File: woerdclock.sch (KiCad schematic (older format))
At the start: 50 parts, among them K1 Sound, K2 IR, K3 CONN_3, K4 CONN_3, P1 Jumper, P2 Jumper, P3 Jumper, P4 CONN_1, P5 CONN_1, P6 CONN_1, P7 CONN_1, SW1 up, SW2 ok, SW3 down, U1 RFM12B, U10 DCF77, U11 DHT, U14 SD-CARD, U2 RTC_MODUL, U3 ARDUINO_MINI_PRO, U6 HC-05, U7 HC-05, U8 ESP8266, U9 10DOF

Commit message: sub-PCBs ready.
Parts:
- removed K4: CONN_3, symbol CONN_3
- removed U3: ARDUINO_MINI_PRO, symbol ARDUINO_MINI_PRO
- added K10, K13, K14, K17, K18, K21, K22, K25, K26, K4, K5, K9: WS2812B_OUT, ~, symbol WS2812B_OUT
- added K11, K15, K19, K23, K27, K6, K7: WS2812B_IN, symbol WS2812B_IN
- added K12, K16, K20, K24, K8: WS2812B_IN, ~, symbol WS2812B_IN
- added P10, P12, P13, P14, P15, P16, P17, P9: CONN_1, symbol CONN_1
- added P11, P8: CONN_3X2, symbol CONN_3X2
- added P18: JP4, symbol CONN_2
- added R20: 200, symbol R
- added U3: ARDUINO_PRO_MICRO, symbol ARDUINO_PRO_MICRO
- added U4: BH1750FVI_MODULE, symbol BH1750FVI_MODULE
- added U5: HOHLSTECKER, ~, symbol HOHLSTECKER
- P1: value Jumper -> JP3
- P2: value Jumper -> JP2
- P3: value Jumper -> JP1
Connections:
- net labels added: Buttons/LDR, RXwlan, TXwlan, WS2811subPCB, rxBT1, rxBT2, txBT1, txBT2
- net labels removed: Buttons, RX1, RX2, RX3, TX1, TX2, TX3
- wire segments 63 -> 143
- no-connect marks 19 -> 21
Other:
- note added: "4x pixel for minutes"
- note added: "BH1750 Light Sensor Module"
- note added: "Platinenverbindung"
- note removed: "Pixel"
- moved on the sheet: C1, C3, K1, K2, K3, P1, R1, R18, R2, R3, R4, R5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

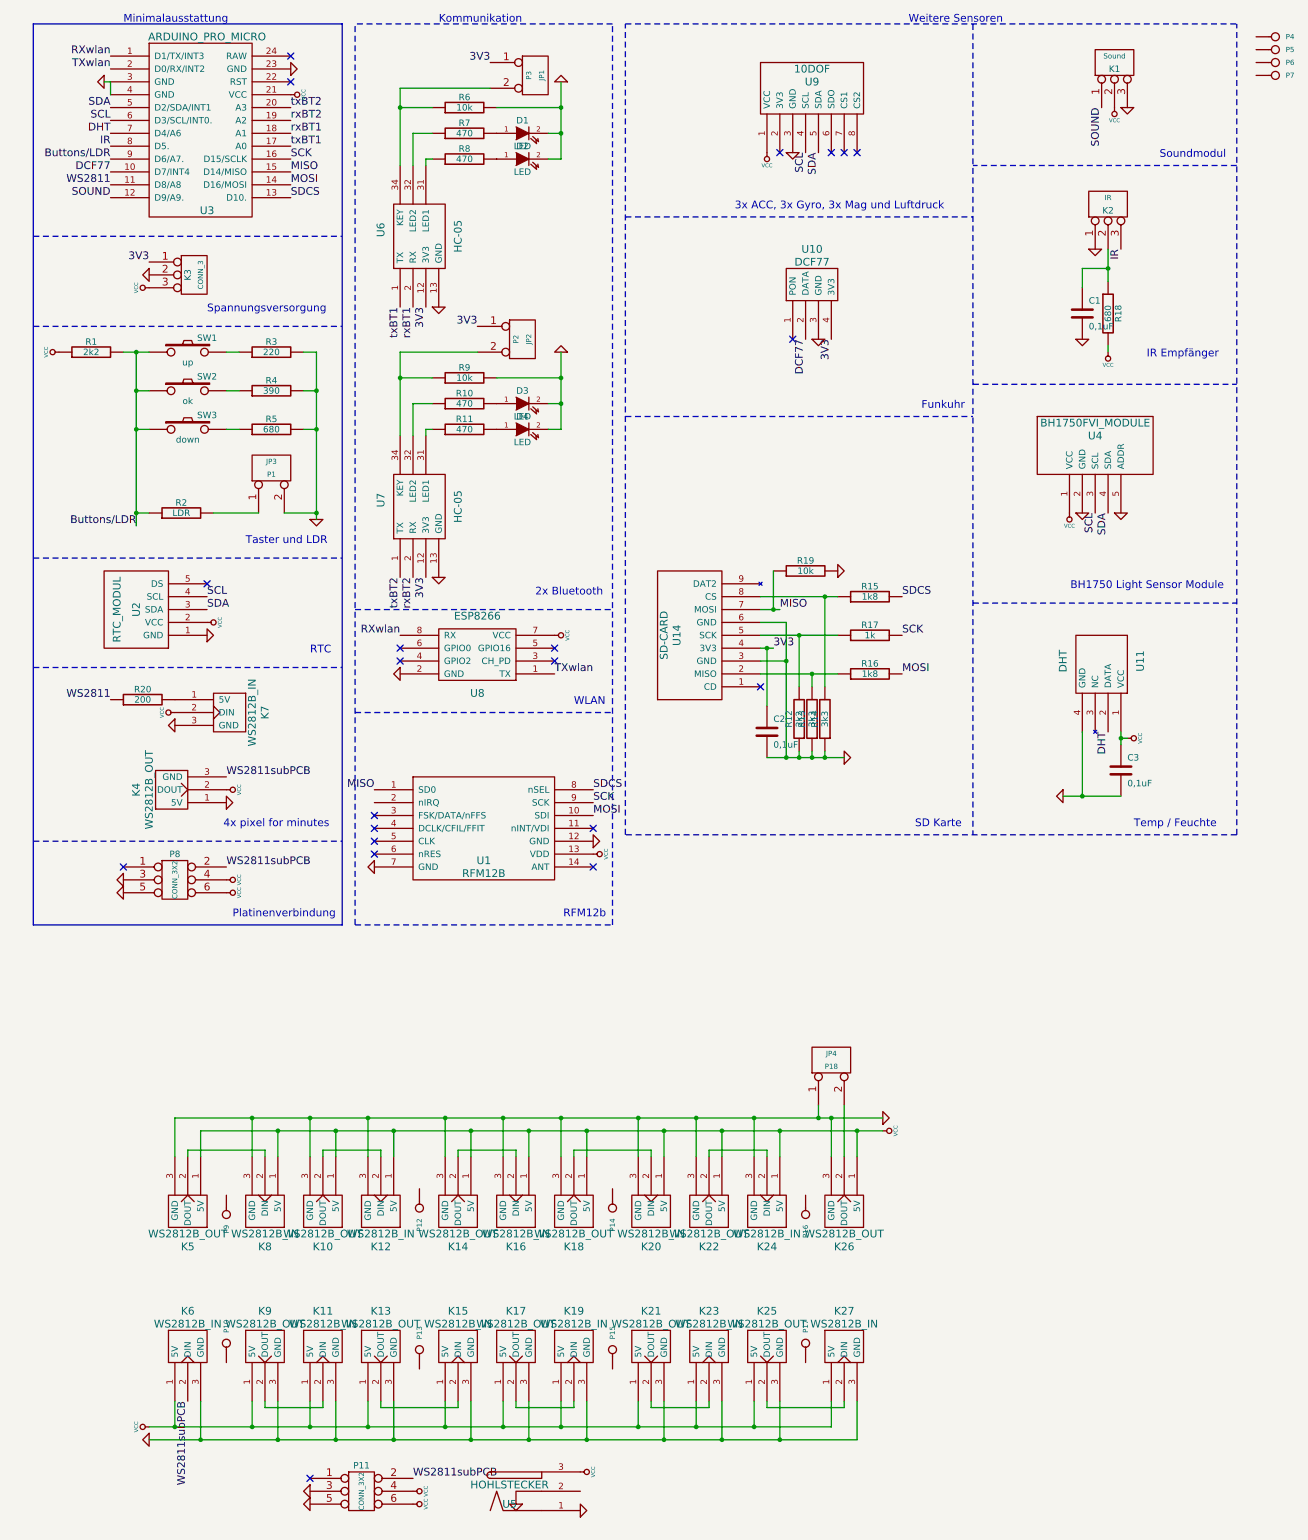
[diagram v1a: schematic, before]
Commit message: I had to rotate the footprints for the WS12B on the sub-PCBs. Cleaning up. RFM12B shares INT4 with DCF77.
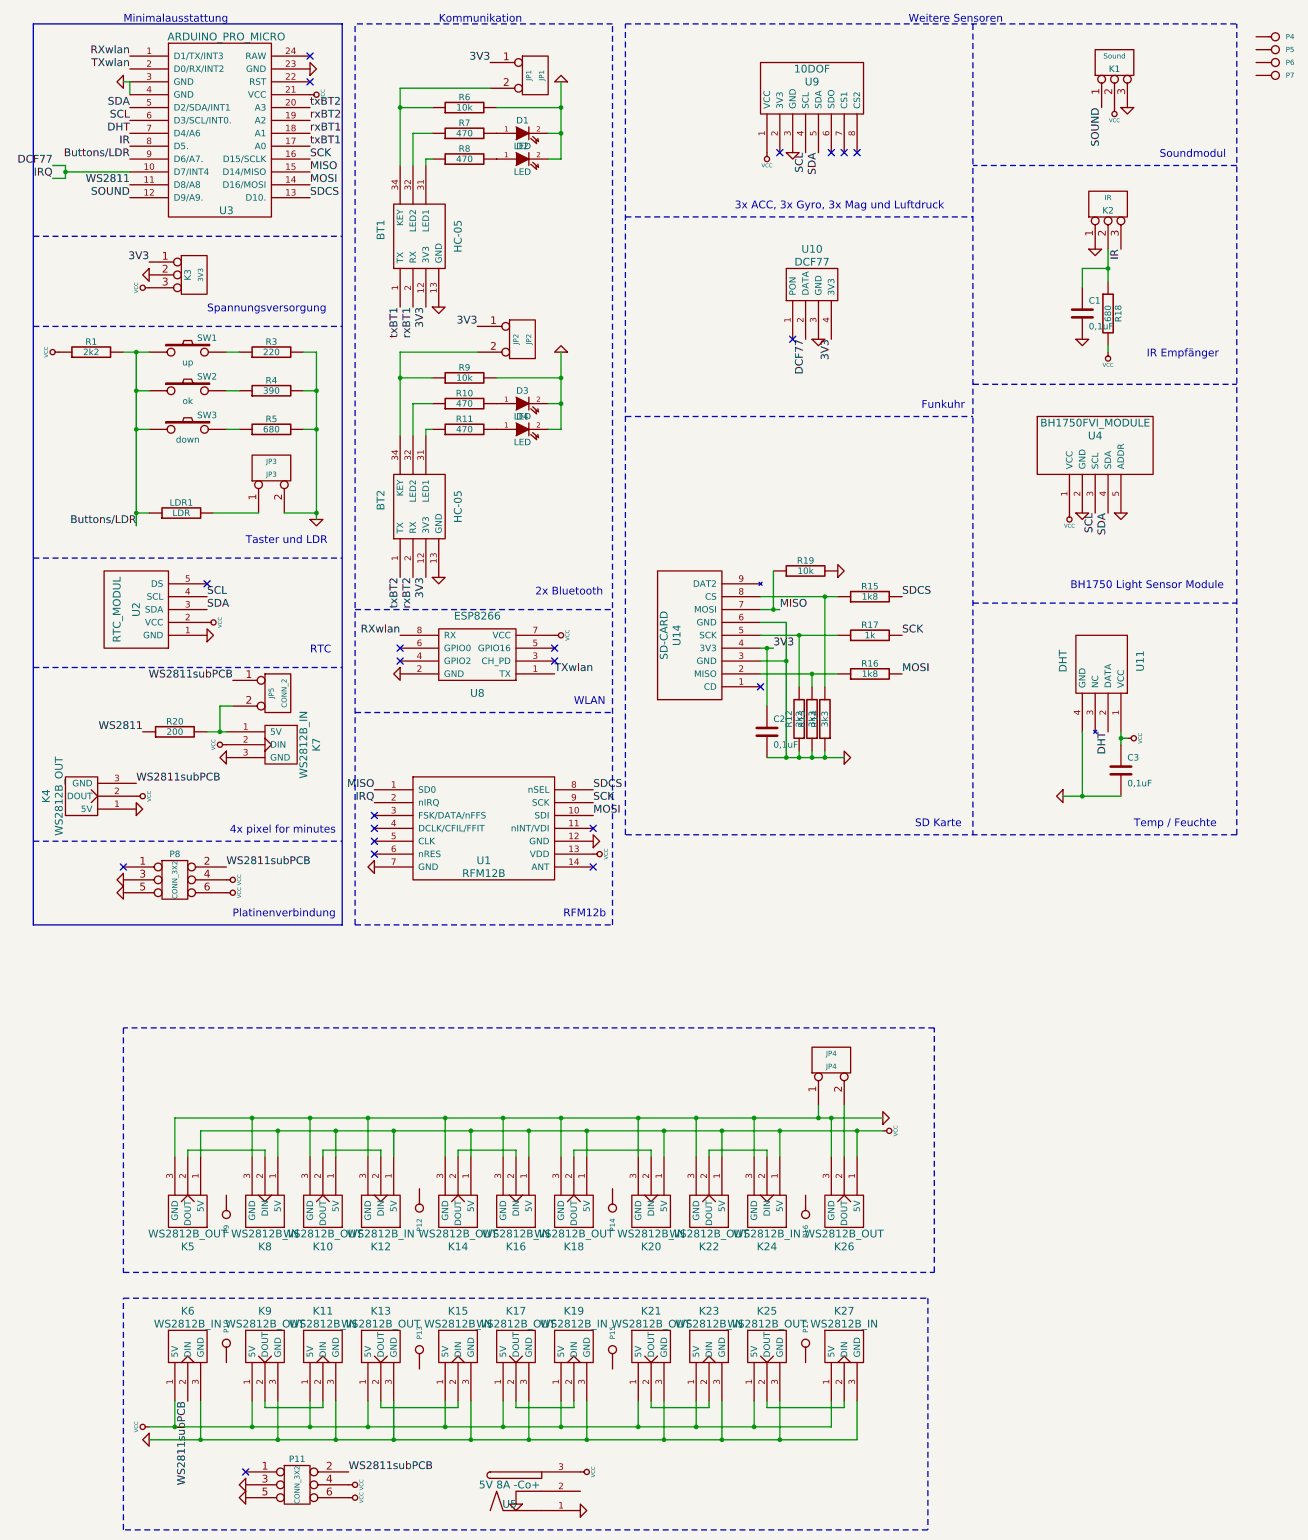
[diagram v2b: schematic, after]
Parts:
- added JP5: CONN_2, symbol CONN_2
- K3: value CONN_3 -> 3V3
- U5: value HOHLSTECKER -> 5V 8A -Co+
- renumbered U6 to BT1, U7 to BT2, P3 to JP1, P2 to JP2, P1 to JP3, P18 to JP4, R2 to LDR1
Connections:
- net DCF77: now also U1.2 (nIRQ)
- net WS2811subPCB: now also JP5.1 (P1)
- net at K7.1 (5V), R20.2: now also JP5.2 (PM)
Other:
- moved on the sheet: K4, K7, P11, R20, U3
